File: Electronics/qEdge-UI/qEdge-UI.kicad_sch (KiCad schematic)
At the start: 20 parts

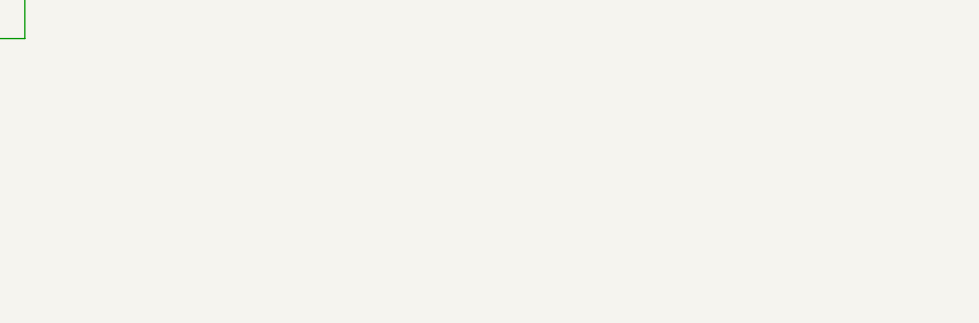
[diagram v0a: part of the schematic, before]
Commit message: added READMEs for Mechanic and Electronic added License in the Electronic schematics restructured Mechanics for better readability and reproducibility
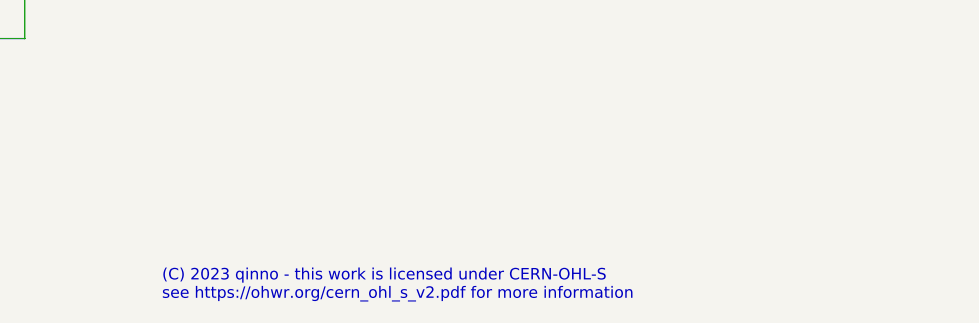
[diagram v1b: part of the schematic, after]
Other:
- note added: "(C) 2023 qinno - this work is licensed under CERN-OHL-S see https://ohwr.org/cern_ohl_s_v2.pdf for more information"
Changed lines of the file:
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@@
+    (effects (font (size 1.27 1.27)) (justify left bottom))
+  )
+  (text "(C) 2023 qinno - this work is licensed under CERN-OHL-S\nsee https://ohwr.org/cern_ohl_s_v2.pdf for more information"
+    (at 238.76 283.21 0)
     (effects (font (size 1.27 1.27)) (justify left bottom))
   )
